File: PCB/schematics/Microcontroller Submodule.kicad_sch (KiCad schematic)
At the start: 7 parts

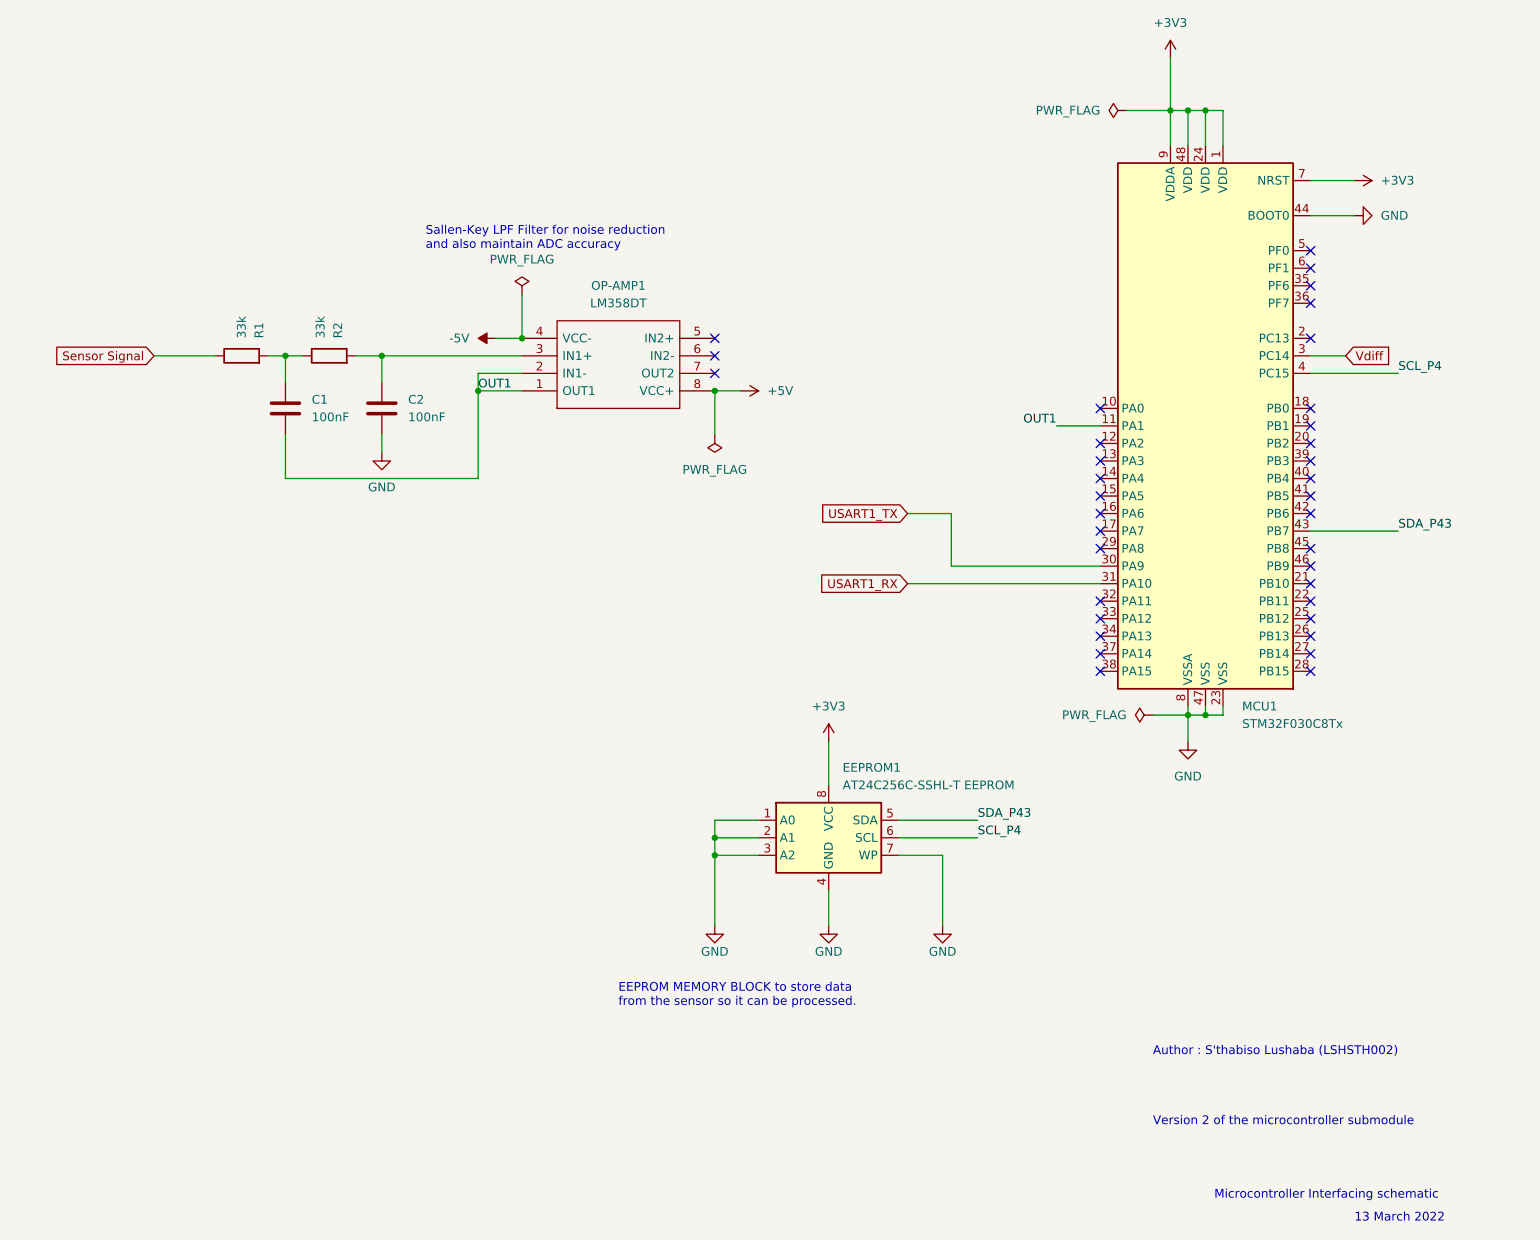
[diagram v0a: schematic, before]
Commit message: updated microcontroller schematic
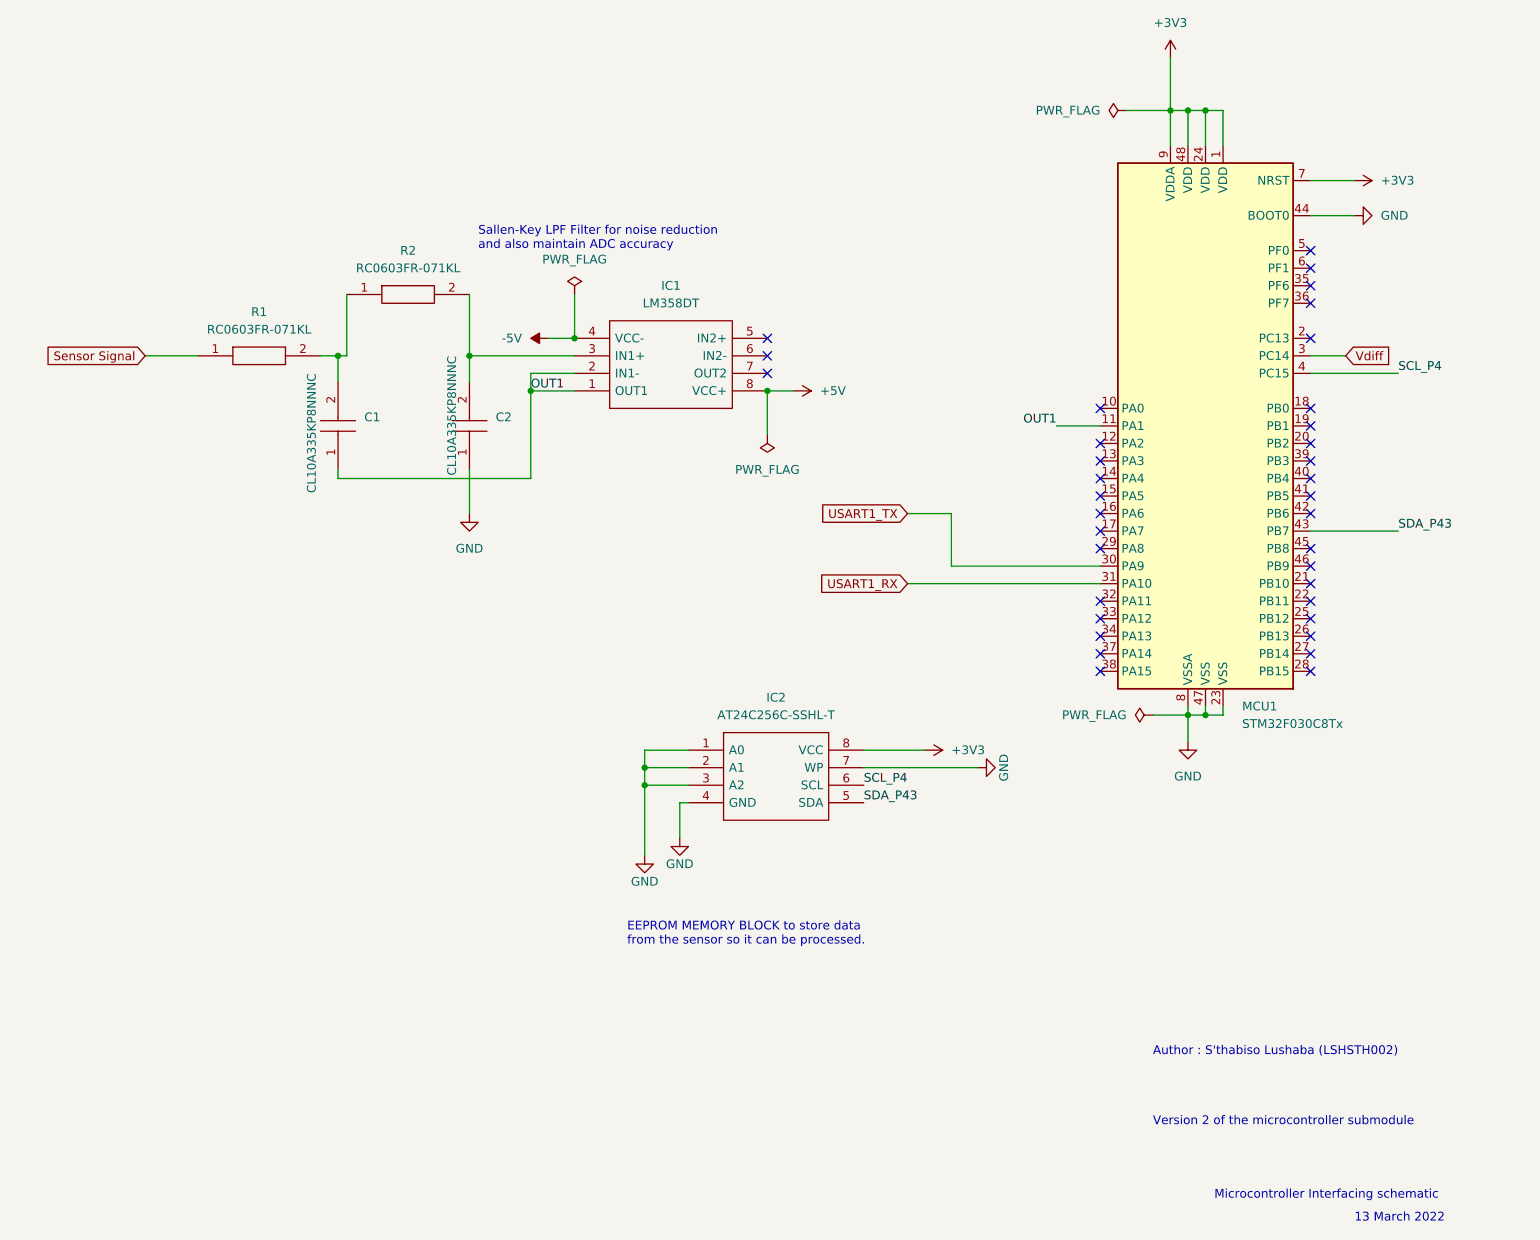
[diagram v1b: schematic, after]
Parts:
- removed C1, C2: 100nF, symbol Device:C
- removed EEPROM1: AT24C256C-SSHL-T EEPROM, symbol Memory_EEPROM:24LC64
- removed OP-AMP1: LM358DT, SOIC127P600X175-8N, symbol LM358DT:LM358DT
- removed R1, R2: 33k, symbol Device:R
- added C1, C2: CL10A335KP8NNNC, SamacSys_Parts:CAPC1608X90N, symbol SamacSys_Parts_Microcontroller:CL10A335KP8NNNC
- added IC1: LM358DT, SamacSys_Parts:SOIC127P600X175-8N, symbol SamacSys_Parts:LM358DT
- added IC2: AT24C256C-SSHL-T, SamacSys_Parts:SOIC127P600X175-8N, symbol SamacSys_Parts_Microcontroller:AT24C256C-SSHL-T
- added R1, R2: RC0603FR-071KL, SamacSys_Parts:RESC1608X55N, symbol SamacSys_Parts_Microcontroller:RC0603FR-071KL
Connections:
- net +3V3: now also IC2.8 (VCC)
- net +5V: now also IC1.8 (VCC+)
- net -5V: now also IC1.4 (VCC-)
- net GND: now also C2.1, IC2.1 (A0), IC2.2 (A1), IC2.3 (A2), IC2.4 (GND), IC2.7 (WP)
- net OUT1: now also C1.1, IC1.1 (OUT1), IC1.2 (IN1-)
- net SCL_P4: now also IC2.6 (SCL)
- net SDA_P43: now also IC2.5 (SDA)
- net Sensor Signal: now also R1.1
- new net: C2.2, IC1.3 (IN1+), R2.2
- new net: C1.2, R1.2, R2.1
